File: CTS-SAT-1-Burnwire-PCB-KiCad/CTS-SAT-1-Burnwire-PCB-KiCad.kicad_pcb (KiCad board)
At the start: 2 copper layers, 50.8 x 22.9 mm, 6 parts, among them J1 feather long, J2 feather short

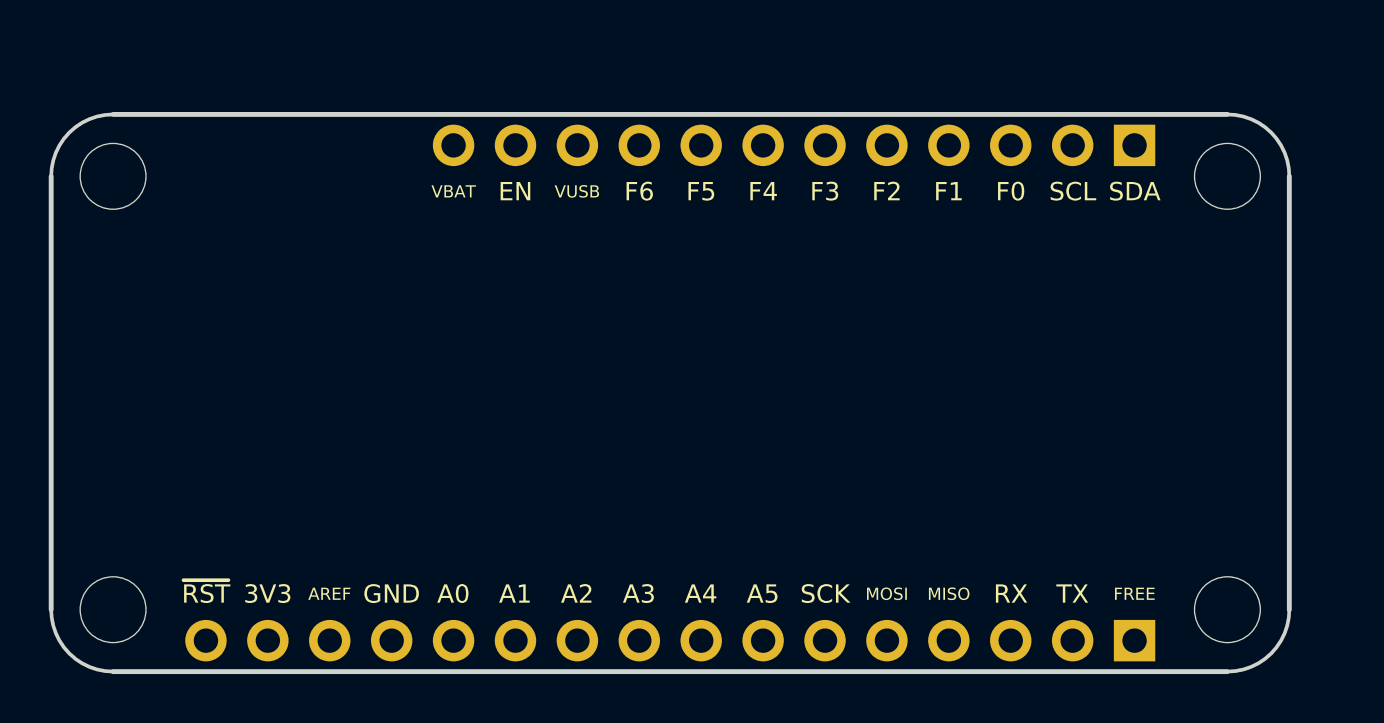
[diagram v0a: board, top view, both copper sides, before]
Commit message: Organized Schematic and PCB Layout
Organized the Schematic to make it more neat and organized the ratsnest of the PCB.
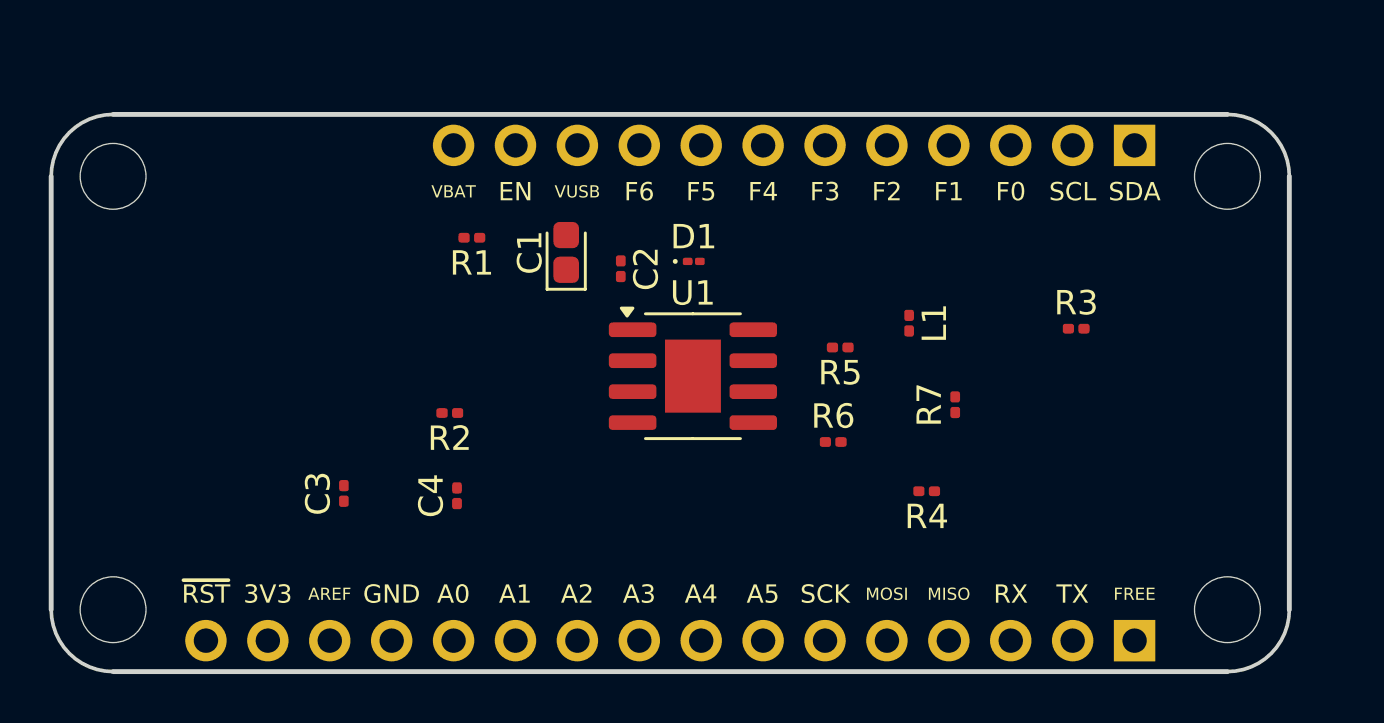
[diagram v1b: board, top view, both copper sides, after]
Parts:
- added C1: 22µ, Capacitor_Tantalum_SMD:CP_EIA-1608-08_AVX-J, F.Cu at (46.5, 31.1)
- added C2: 0.1µ, Capacitor_SMD:C_0201_0603Metric, F.Cu at (48.8, 31.7)
- added C3: 47µ, Capacitor_SMD:C_0201_0603Metric, F.Cu at (37.4, 41.0)
- added C4: 47µ, Capacitor_SMD:C_0201_0603Metric, F.Cu at (42.0, 41.0)
- added D1: B540C, Diode_SMD:D_01005_0402Metric, F.Cu at (51.8, 31.4)
- added L1: 2.5µ, Inductor_SMD:L_0201_0603Metric, F.Cu at (60.6, 34.0)
- added R1: 10.2k, Resistor_SMD:R_0201_0603Metric, F.Cu at (42.7, 30.5)
- added R2: 10.2k, Resistor_SMD:R_0201_0603Metric, F.Cu at (41.8, 37.6)
- added R3: 1.5, Resistor_SMD:R_0201_0603Metric, F.Cu at (67.5, 34.2)
- added R4: 33k, Resistor_SMD:R_0201_0603Metric, F.Cu at (61.3, 40.9)
- added R5: 10.2k, Resistor_SMD:R_0201_0603Metric, F.Cu at (57.8, 35.0)
- added R6: 10k, Resistor_SMD:R_0201_0603Metric, F.Cu at (57.5, 38.8)
- added R7: 0.5, Resistor_SMD:R_0201_0603Metric, F.Cu at (62.5, 37.3)
- added U1: ADP2303ARDZ, Package_SO:SOIC-8-1EP_3.9x4.9mm_P1.27mm_EP2.29x3mm, F.Cu at (51.7, 36.1)
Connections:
- J2 pad 11: /EN -> EN3V
- J2 pad 12: /VBAT -> Vin

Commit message: Low Side Switch Burnwire Design
Added 350mA current limiting low side switch
Added footprints for two thru-hole and two SMD burn resistors
Added Picoblade connectors
Added LEDs and test switches
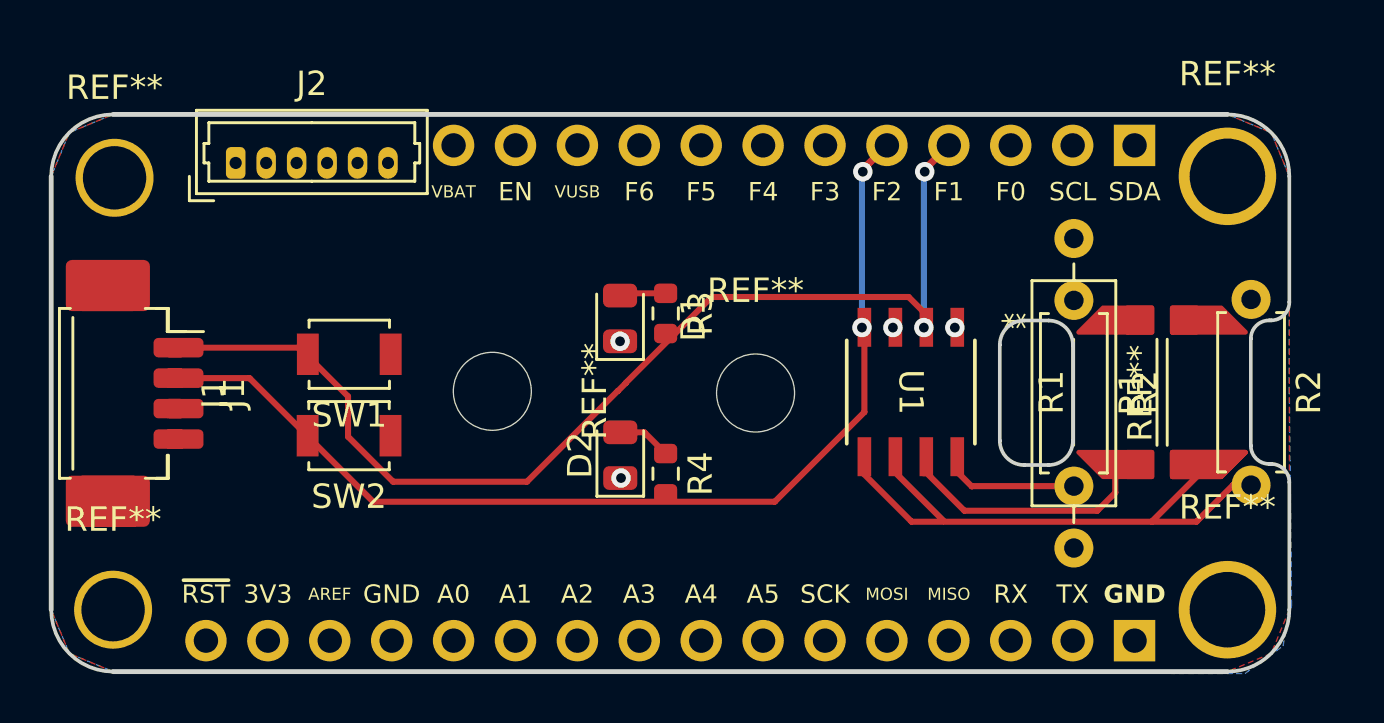
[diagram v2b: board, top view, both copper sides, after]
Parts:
- removed C1: 22µ, Capacitor_Tantalum_SMD:CP_EIA-1608-08_AVX-J
- removed C2: 0.1µ, Capacitor_SMD:C_0201_0603Metric
- removed C3, C4: 47µ, Capacitor_SMD:C_0201_0603Metric
- removed L1: 2.5µ, Inductor_SMD:L_0201_0603Metric
- removed the R1 at (42.7, 30.5)
- removed the R2 at (41.8, 37.6)
- removed R5: 10.2k, Resistor_SMD:R_0201_0603Metric
- removed R6: 10k, Resistor_SMD:R_0201_0603Metric
- removed R7: 0.5, Resistor_SMD:R_0201_0603Metric
- added D2: LED_RED, LED_SMD:LED_0805_2012Metric, F.Cu at (48.8, 39.4)
- added J1: Molex_PicoBlade_53398-0471_1x04-1MP_P1.25mm_Vertical, Connector_Molex:Molex_PicoBlade_53261-0471_1x04-1MP_P1.25mm_Horizontal, F.Cu at (28.4, 36.8)
- added J1: Molex_PicoBlade_53398-0471_1x04-1MP_P1.25mm_Vertical, Connector_Molex:Molex_PicoBlade_53398-0471_1x04-1MP_P1.25mm_Vertical, F.Cu at (29.0, 36.8)
- added J2: Molex_PicoBlade_53047-0610_1x06_P1.25mm_Vertical, Connector_Molex:Molex_PicoBlade_53047-0610_1x06_P1.25mm_Vertical, F.Cu at (33.0, 27.4)
- added R1: R_2512_6332Metric, Resistor_THT:R_Axial_DIN0207_L6.3mm_D2.5mm_P7.62mm_Horizontal, F.Cu at (67.4, 33.0)
- added R1: R_2512_6332Metric, Resistor_SMD:R_2512_6332Metric, F.Cu at (69.1, 36.8)
- added R2: R, Resistor_THT:R_Axial_DIN0207_L6.3mm_D2.5mm_P7.62mm_Horizontal, F.Cu at (74.6, 33.0)
- added R2: R, Resistor_SMD:R_2512_6332Metric, F.Cu at (72.9, 36.8)
- added REF**: MountingHole_3.2mm_M3, MountingHole:MountingHole_3.2mm_M3, F.Cu at (54.3, 36.8)
- added REF**: MountingHole_3.2mm_M3, MountingHole:MountingHole_3.2mm_M3, F.Cu at (43.5, 36.8)
- added REF**: R_Axial_DIN0309_L9.0mm_D3.2mm_P12.70mm_Horizontal, Resistor_THT:R_Axial_DIN0309_L9.0mm_D3.2mm_P12.70mm_Horizontal, F.Cu at (67.4, 30.5)
- added SW1: SW_SPST, Button_Switch_SMD:SW_SPST_B3U-1000P, F.Cu at (37.6, 35.2)
- added SW2: SW_SPST, Button_Switch_SMD:SW_SPST_B3U-1000P, F.Cu at (37.6, 38.6)
- D1: value B540C -> LED_RED_IN1; footprint Diode_SMD:D_01005_0402Metric -> LED_SMD:LED_0805_2012Metric
- R3: value 1.5 -> 100; footprint Resistor_SMD:R_0201_0603Metric -> Resistor_SMD:R_0603_1608Metric
- R4: value 33k -> 100; footprint Resistor_SMD:R_0201_0603Metric -> Resistor_SMD:R_0603_1608Metric
- REF** (x2): value MountingHole_2.7mm_M2.5 -> MountingHole_3.2mm_M3; footprint MountingHole:MountingHole_2.7mm_M2.5 -> MountingHole:MountingHole_3.2mm_M3
- U1: value ADP2303ARDZ -> BTS3405GXUMA1; footprint Package_SO:SOIC-8-1EP_3.9x4.9mm_P1.27mm_EP2.29x3mm -> footprints2:PG-DSO-8-25_INF
- moved R3 16.9 mm to (50.6, 33.6), turned to -90 degrees
- moved R4 10.7 mm to (50.6, 40.1), turned to -90 degrees
- moved U1 8.96 mm to (60.7, 36.8), turned to -90 degrees
- moved D1 3.82 mm to (48.7, 33.8), turned to 90 degrees
- moved REF** 0.08 mm to (28.0, 28.0)
- renumbered J1 to J3, J2 to J4
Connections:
- J3 pad 1: /FREE -> GND
- J4 pad 4: /F1 -> IN1
- J4 pad 5: /F2 -> IN2
- R3 pad 1: Net-(R3-Pad1) -> Net-(D1-A)
- R3 pad 2: Net-(C3-Pad1) -> IN1
- R4 pad 1: Net-(U1-FB) -> Net-(D2-A)
- R4 pad 2: Net-(C3-Pad1) -> IN2
- U1 pad 1: Net-(U1-BST) -> GND
- U1 pad 2: Net-(U1-Vin) -> IN1
- U1 pad 3: Net-(U1-EN) -> GND
- U1 pad 4: Net-(U1-PGOOD) -> IN2
- U1 pad 5: Net-(U1-FB) -> Net-(R2-Pad2)
- U1 pad 6: unconnected-(U1-NC-Pad6) -> Net-(R2-Pad2)
- U1 pad 7: GND -> Net-(R1-Pad2)
- U1 pad 8: Net-(D1-A) -> Net-(R1-Pad2)
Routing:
- net IN1: track 0.00 -> 45.9 mm, vias 0 -> 2
- net IN2: track 0.00 -> 43.5 mm, vias 0 -> 2
- net Net-(R2-Pad2): track 0.00 -> 24.8 mm
- net Net-(R1-Pad2): track 0.00 -> 17.9 mm
- net Net-(D2-A): track 0.00 -> 2.22 mm
- net Net-(D1-A): track 0.00 -> 1.91 mm
- net GND: vias 0 -> 4
- added copper zone on B.Cu, net GND
- added copper zone on F.Cu, net Vin
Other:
- outline, holes or cut-outs redrawn
- board text removed: "FREE"
